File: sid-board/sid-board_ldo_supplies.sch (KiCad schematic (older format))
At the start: 12 parts, among them J1 ICM_CONN, J2 SID_CONN, J3 5V/GND, J4 3.3V/GND, J5 SPI, J6 UARTAB/IRQ, U1 SC16IS752IPW, U2 LM2596MODULE, U3 PCA82C250, U4 PCA82C250

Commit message: Working on new mostly-SMD version, switched to independant LDOs, added oscillator circuit.
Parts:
- removed U2: LM2596MODULE, sid-board:LM2596-MODULE, symbol local_symbols:LM2596MODULE
- added C2, C3: 18pF, Capacitor_SMD:C_0805_2012Metric_Pad1.15x1.40mm_HandSolder, symbol Device:C_Small
- added C4: 100nF, Capacitor_SMD:C_0805_2012Metric_Pad1.15x1.40mm_HandSolder, symbol Device:C_Small
- added R2: 1M, Resistor_SMD:R_0805_2012Metric_Pad1.15x1.40mm_HandSolder, symbol Device:R_Small
- added U2: MCP1703A-3302_SOT223, Package_TO_SOT_SMD:SOT-223-3_TabPin2, symbol Regulator_Linear:MCP1703A-3302_SOT223
- added U5: MCP1703A-5002_SOT223, Package_TO_SOT_SMD:SOT-223-3_TabPin2, symbol Regulator_Linear:MCP1703A-5002_SOT223
- added Y1: 14.7456MHz, sid-board:Euroquarts 14.7456MHz Crystal ±30ppm SMD 2-Pin 12.4 x 4.5 x 4.2mm, symbol Device:Crystal
- C1: footprint Capacitor_THT:C_Rect_L7.2mm_W2.5mm_P5.00mm_FKS2_FKP2_MKS2_MKP2 -> Capacitor_SMD:C_0805_2012Metric_Pad1.15x1.40mm_HandSolder
- J3: value 5V/GND -> 5V OUT
- J4: value 3.3V/GND -> 3.3V OUT
- R1: footprint Resistor_THT:R_Axial_DIN0207_L6.3mm_D2.5mm_P7.62mm_Horizontal -> Resistor_SMD:R_0805_2012Metric_Pad1.15x1.40mm_HandSolder
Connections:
- net labels added: XTAL1, XTAL2
- wire segments 64 -> 70
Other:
- note added: "3.3V SUPPLY LDO"
- note added: "5V SUPPLY LDO"
- note added: "TODO:\nADD XTAL1/2 OSCILLATOR CIRCUIT\nADD LDO VOLTAGE INPUT for U1"
- note added: "TOTAL ESTIMATED MAX. CURRENT = 230mA\n3.3V U1 SUPPLY = 20mA peak (2x rated max)\n5V U3/U2 SUPPLY = 210mA peak (1.5x rated max)"
- moved on the sheet: C1, J3
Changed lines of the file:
@@
 Text GLabel 2200 2500 0    50   Input ~ 0
 GND
-$Comp
-L local_symbols:LM2596MODULE U2
-U 1 1 5E29B6B7
-P 2650 4700
-F 0 "U2" H 2650 4925 50  0000 C CNN
-F 1 "LM2596MODULE" H 2650 4834 50  0000 C CNN
-F 2 "sid-board:LM2596-MODULE" H 2650 4700 50  0001 C CNN
-F 3 "" H 2650 4700 50  0001 C CNN
-	1    2650 4700
-	1    0    0    -1
-$EndComp
-Text GLabel 2150 4850 0    50   Input ~ 0
-GND
-Text GLabel 3150 4850 2    50   Input ~ 0
-GND
-Text GLabel 2150 4700 0    50   Input ~ 0
+Text GLabel 1700 5250 0    50   Input ~ 0
+GND
+Text GLabel 1400 4950 0    50   Input ~ 0
 VIN
-Text GLabel 3150 4700 2    50   Input ~ 0
+Text GLabel 3400 4950 2    50   Input ~ 0
 VDD_5V
 Text GLabel 2200 3500 0    50   Input ~ 0
@@
 L Device:C_Small C1
 U 1 1 5E2BAD29
-P 3500 3000
-F 0 "C1" V 3271 3000 50  0000 C CNN
-F 1 "100nF" V 3362 3000 50  0000 C CNN
-F 2 "Capacitor_THT:C_Rect_L7.2mm_W2.5mm_P5.00mm_FKS2_FKP2_MKS2_MKP2" H 3500 3000 50  0001 C CNN
-F 3 "~" H 3500 3000 50  0001 C CNN
-	1    3500 3000
-	0    1    1    0
-$EndComp
-Wire Wire Line
-	3950 2450 3400 2450
-Wire Wire Line
-	3600 3000 4700 3000
-Wire Wire Line
-	4700 3000 4700 2900
+P 3300 5250
+F 0 "C1" V 3071 5250 50  0000 C CNN
+F 1 "100nF" V 3162 5250 50  0000 C CNN
+F 2 "Capacitor_SMD:C_0805_2012Metric_Pad1.15x1.40mm_HandSolder" H 3300 5250 50  0001 C CNN
+F 3 "~" H 3300 5250 50  0001 C CNN
+	1    3300 5250
+	0    1    1    0
+$EndComp
 Wire Wire Line
 	3950 3300 3900 3300
@@
 Wire Wire Line
 	5500 3200 6300 3200
-Text GLabel 3800 4700 3    50   Input ~ 0
+Text GLabel 4250 4700 3    50   Input ~ 0
 VDD_5V
-Text GLabel 3900 4700 3    50   Input ~ 0
+Text GLabel 4350 4700 3    50   Input ~ 0
 GND
 Text GLabel 4850 4700 3    50   Input ~ 0
@@
 L Connector:Conn_01x02_Male J3
 U 1 1 5E30F0FD
-P 3900 4500
-F 0 "J3" V 3962 4544 50  0000 L CNN
-F 1 "5V/GND" V 4053 4544 50  0000 L CNN
-F 2 "Connector_PinHeader_2.54mm:PinHeader_1x02_P2.54mm_Vertical" H 3900 4500 50  0001 C CNN
-F 3 "~" H 3900 4500 50  0001 C CNN
-	1    3900 4500
+P 4350 4500
+F 0 "J3" V 4412 4544 50  0000 L CNN
+F 1 "5V OUT" V 4503 4544 50  0000 L CNN
+F 2 "Connector_PinHeader_2.54mm:PinHeader_1x02_P2.54mm_Vertical" H 4350 4500 50  0001 C CNN
+F 3 "~" H 4350 4500 50  0001 C CNN
+	1    4350 4500
 	0    1    1    0
 $EndComp
@@
 P 4850 4500
 F 0 "J4" V 4912 4544 50  0000 L CNN
-F 1 "3.3V/GND" V 5003 4544 50  0000 L CNN
+F 1 "3.3V OUT" V 5003 4544 50  0000 L CNN
 F 2 "Connector_PinHeader_2.54mm:PinHeader_1x02_P2.54mm_Vertical" H 4850 4500 50  0001 C CNN
 F 3 "~" H 4850 4500 50  0001 C CNN
@@
 F 0 "R1" H 6709 3846 50  0000 L CNN
 F 1 "1K" H 6709 3755 50  0000 L CNN
-F 2 "Resistor_THT:R_Axial_DIN0207_L6.3mm_D2.5mm_P7.62mm_Horizontal" H 6650 3800 50  0001 C CNN
+F 2 "Resistor_SMD:R_0805_2012Metric_Pad1.15x1.40mm_HandSolder" H 6650 3800 50  0001 C CNN
 F 3 "~" H 6650 3800 50  0001 C CNN
 	1    6650 3800
@@
 	6100 2850 6100 4000
 Wire Wire Line
-	3400 2450 3400 3000
-Wire Wire Line
-	3950 2300 3950 2450
-Wire Wire Line
 	3950 2300 3900 2300
 Wire Wire Line
 	4700 2300 4700 2350
+Text Notes 5600 2000 0    50   ~ 0
+TODO:\nADD XTAL1/2 OSCILLATOR CIRCUIT\nADD LDO VOLTAGE INPUT for U1
+Text GLabel 3100 5250 0    50   Input ~ 0
+GND
+Text GLabel 2000 4950 2    50   Input ~ 0
+VDD_3.3V
+Text Notes 1450 4450 0    50   ~ 0
+TOTAL ESTIMATED MAX. CURRENT = 230mA\n3.3V U1 SUPPLY = 20mA peak (2x rated max)\n5V U3/U2 SUPPLY = 210mA peak (1.5x rated max)
+$Comp
+L Regulator_Linear:MCP1703A-3302_SOT223 U2
+U 1 1 5E2845BD
+P 1700 4950
+F 0 "U2" H 1700 5192 50  0000 C CNN
+F 1 "MCP1703A-3302_SOT223" H 1700 5101 50  0000 C CNN
+F 2 "Package_TO_SOT_SMD:SOT-223-3_TabPin2" H 1700 5150 50  0001 C CNN
+F 3 "http://ww1.microchip.com/downloads/en/DeviceDoc/20005122B.pdf" H 1700 4900 50  0001 C CNN
+	1    1700 4950
+	1    0    0    -1
+$EndComp
+$Comp
+L Regulator_Linear:MCP1703A-5002_SOT223 U5
+U 1 1 5E285FEA
+P 3100 4950
+F 0 "U5" H 3100 5192 50  0000 C CNN
+F 1 "MCP1703A-5002_SOT223" H 3100 5101 50  0000 C CNN
+F 2 "Package_TO_SOT_SMD:SOT-223-3_TabPin2" H 3100 5150 50  0001 C CNN
+F 3 "http://ww1.microchip.com/downloads/en/DeviceDoc/20005122B.pdf" H 3100 4900 50  0001 C CNN
+	1    3100 4950
+	1    0    0    -1
+$EndComp
+Text GLabel 2800 4950 0    50   Input ~ 0
+VIN
+Text Notes 1400 4650 0    50   ~ 10
+3.3V SUPPLY LDO
+Text Notes 2800 4650 0    50   ~ 10
+5V SUPPLY LDO
+$Comp
+L Device:Crystal Y1
+U 1 1 5E2B8361
+P 7400 3000
+F 0 "Y1" H 7400 3268 50  0000 C CNN
+F 1 "14.7456MHz" H 7400 3177 50  0000 C CNN
+F 2 "sid-board:Euroquarts 14.7456MHz Crystal ±30ppm SMD 2-Pin 12.4 x 4.5 x 4.2mm" H 7400 3000 50  0001 C CNN
+F 3 "~" H 7400 3000 50  0001 C CNN
+	1    7400 3000
+	1    0    0    -1
+$EndComp
+$Comp
+L Device:R_Small R2
+U 1 1 5E2B87B7
+P 7400 3350
+F 0 "R2" V 7204 3350 50  0000 C CNN
+F 1 "1M" V 7295 3350 50  0000 C CNN
+F 2 "Resistor_SMD:R_0805_2012Metric_Pad1.15x1.40mm_HandSolder" H 7400 3350 50  0001 C CNN
+F 3 "~" H 7400 3350 50  0001 C CNN
+	1    7400 3350
+	0    1    1    0
+$EndComp
+$Comp
+L Device:C_Small C2
+U 1 1 5E2B9259
+P 7250 3600
+F 0 "C2" H 7342 3646 50  0000 L CNN
+F 1 "18pF" H 7342 3555 50  0000 L CNN
+F 2 "Capacitor_SMD:C_0805_2012Metric_Pad1.15x1.40mm_HandSolder" H 7250 3600 50  0001 C CNN
+F 3 "~" H 7250 3600 50  0001 C CNN
+	1    7250 3600
+	1    0    0    -1
+$EndComp
+$Comp
+L Device:C_Small C3
+U 1 1 5E2BA581
+P 7550 3600
+F 0 "C3" H 7642 3646 50  0000 L CNN
+F 1 "18pF" H 7642 3555 50  0000 L CNN
+F 2 "Capacitor_SMD:C_0805_2012Metric_Pad1.15x1.40mm_HandSolder" H 7550 3600 50  0001 C CNN
+F 3 "~" H 7550 3600 50  0001 C CNN
+	1    7550 3600
+	1    0    0    -1
+$EndComp
+Wire Wire Line
+	7250 3000 7250 3350
+Wire Wire Line
+	7250 3350 7300 3350
+Wire Wire Line
+	7250 3350 7250 3500
+Connection ~ 7250 3350
+Wire Wire Line
+	7550 3000 7550 3350
+Wire Wire Line
+	7550 3350 7500 3350
+Wire Wire Line
+	7250 3700 7550 3700
+Wire Wire Line
+	7550 3350 7550 3500
+Connection ~ 7550 3350
+Text GLabel 7400 3700 3    50   Input ~ 0
+GND
+Text GLabel 7550 3000 2    50   Input ~ 10
+XTAL1
+Text GLabel 7250 3000 0    50   Input ~ 10
+XTAL2
+Text GLabel 5500 2900 0    50   Input ~ 10
+XTAL1
+Text GLabel 5500 3000 0    50   Input ~ 10
+XTAL2
+$Comp
+L Device:C_Small C4
+U 1 1 5E29894F
+P 1900 5250
+F 0 "C4" V 1671 5250 50  0000 C CNN
+F 1 "100nF" V 1762 5250 50  0000 C CNN
+F 2 "Capacitor_SMD:C_0805_2012Metric_Pad1.15x1.40mm_HandSolder" H 1900 5250 50  0001 C CNN
+F 3 "~" H 1900 5250 50  0001 C CNN
+	1    1900 5250
+	0    1    1    0
+$EndComp
+Wire Wire Line
+	2000 4950 2000 5250
+Wire Wire Line
+	1800 5250 1700 5250
+Wire Wire Line
+	3100 5250 3200 5250
+Wire Wire Line
+	3400 5250 3400 4950
 $EndSCHEMATC

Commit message: Re-did PCB layout, signifcantly smaller now.
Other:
- note removed: "TODO:\nADD XTAL1/2 OSCILLATOR CIRCUIT\nADD LDO VOLTAGE INPUT for U1"
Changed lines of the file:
@@
 Wire Wire Line
 	4700 2300 4700 2350
-Text Notes 5600 2000 0    50   ~ 0
-TODO:\nADD XTAL1/2 OSCILLATOR CIRCUIT\nADD LDO VOLTAGE INPUT for U1
 Text GLabel 3100 5250 0    50   Input ~ 0
 GND

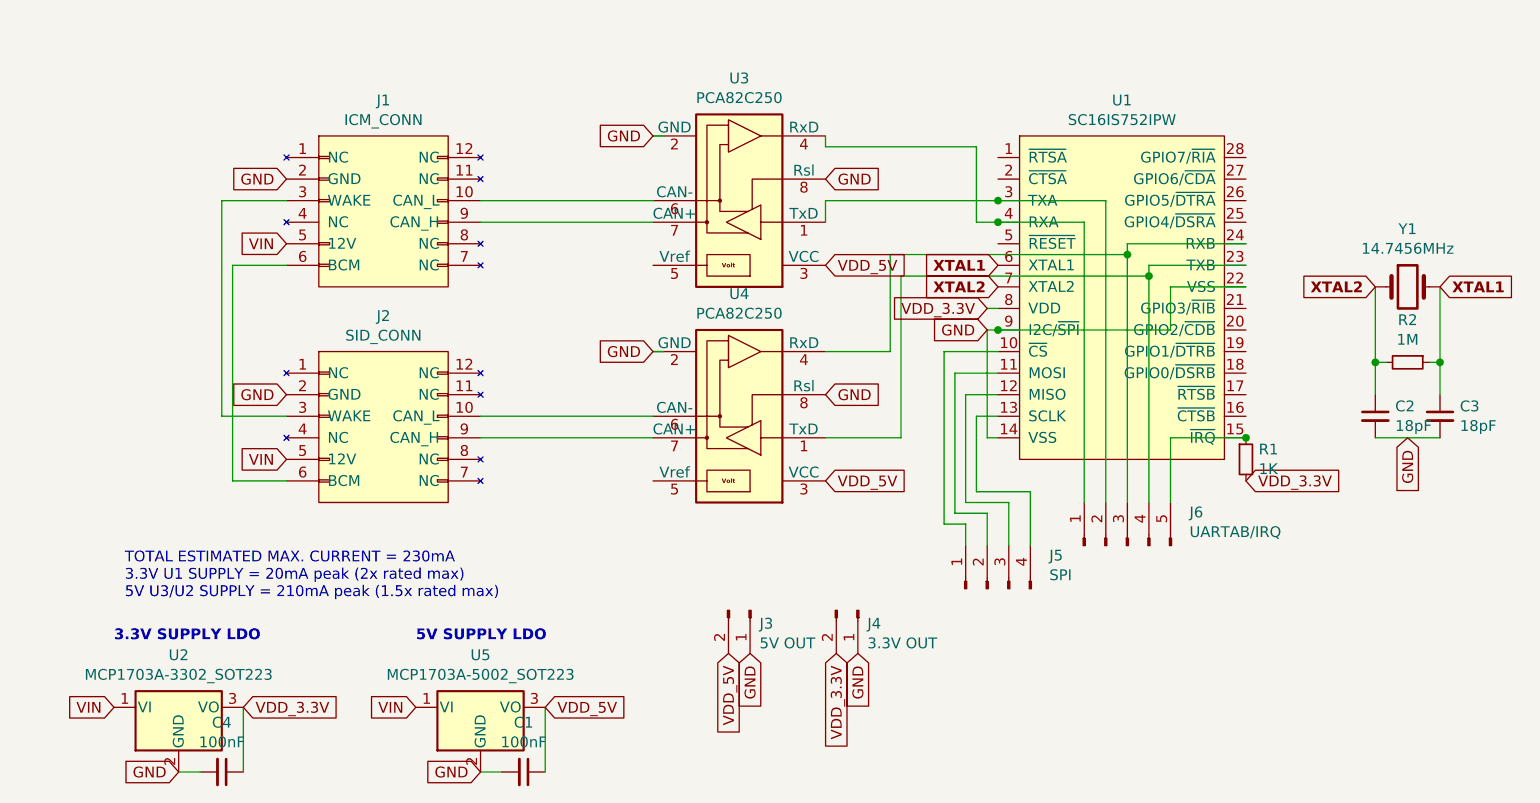
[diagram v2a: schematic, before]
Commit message: Autorouted vs Manual routed. Thinking about adding DIP switch.
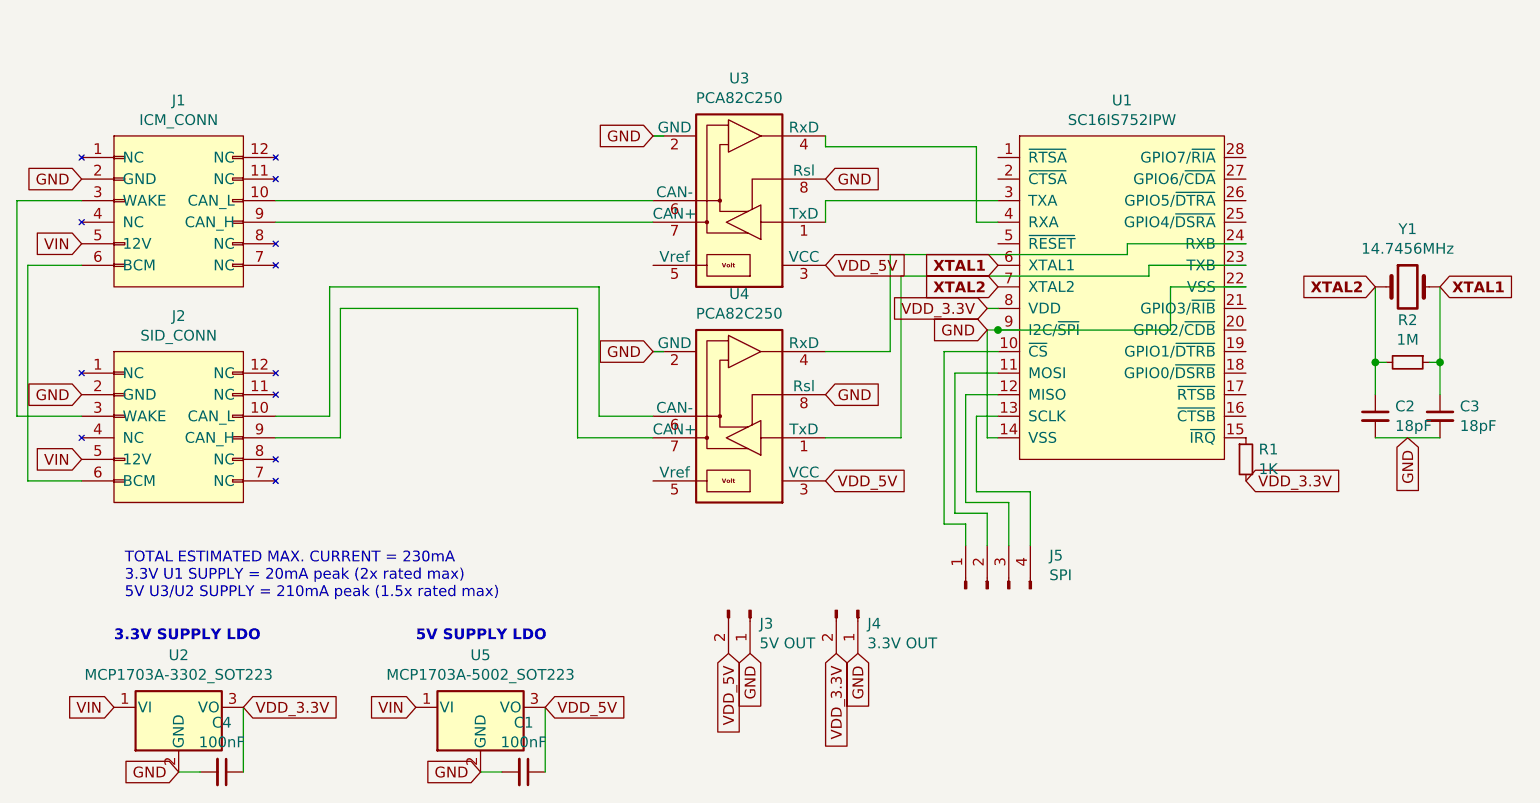
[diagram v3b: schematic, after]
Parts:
- removed J6: UARTAB/IRQ, Connector_PinHeader_2.54mm:PinHeader_1x05_P2.54mm_Vertical, symbol Connector:Conn_01x05_Male
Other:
- moved on the sheet: J1, J2
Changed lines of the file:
@@
 L local_symbols:Conn_02x06_SAAB_SID_HPD J1
 U 1 1 5E210180
-P 2650 2600
-F 0 "J1" H 2650 3065 50  0000 C CNN
-F 1 "ICM_CONN" H 2650 2974 50  0000 C CNN
-F 2 "sid-board:SAAB_SID_CONNECTOR_HEADER" H 2400 2600 50  0001 C CNN
-F 3 "~" H 2400 2600 50  0001 C CNN
-	1    2650 2600
+P 1700 2600
+F 0 "J1" H 1700 3065 50  0000 C CNN
+F 1 "ICM_CONN" H 1700 2974 50  0000 C CNN
+F 2 "sid-board:SAAB_SID_CONNECTOR_HEADER" H 1450 2600 50  0001 C CNN
+F 3 "~" H 1450 2600 50  0001 C CNN
+	1    1700 2600
 	1    0    0    -1
 $EndComp
@@
 L local_symbols:Conn_02x06_SAAB_SID_HPD J2
 U 1 1 5E211BEE
-P 2650 3600
-F 0 "J2" H 2650 4065 50  0000 C CNN
-F 1 "SID_CONN" H 2650 3974 50  0000 C CNN
-F 2 "sid-board:SAAB_SID_CONNECTOR_HEADER" H 2400 3600 50  0001 C CNN
-F 3 "~" H 2400 3600 50  0001 C CNN
-	1    2650 3600
-	1    0    0    -1
-$EndComp
-Text GLabel 2200 2800 0    50   Input ~ 0
+P 1700 3600
+F 0 "J2" H 1700 4065 50  0000 C CNN
+F 1 "SID_CONN" H 1700 3974 50  0000 C CNN
+F 2 "sid-board:SAAB_SID_CONNECTOR_HEADER" H 1450 3600 50  0001 C CNN
+F 3 "~" H 1450 3600 50  0001 C CNN
+	1    1700 3600
+	1    0    0    -1
+$EndComp
+Text GLabel 1250 2800 0    50   Input ~ 0
 VIN
-Text GLabel 2200 2500 0    50   Input ~ 0
+Text GLabel 1250 2500 0    50   Input ~ 0
 GND
 Text GLabel 1700 5250 0    50   Input ~ 0
@@
 Text GLabel 3400 4950 2    50   Input ~ 0
 VDD_5V
-Text GLabel 2200 3500 0    50   Input ~ 0
-GND
-Text GLabel 2200 3800 0    50   Input ~ 0
+Text GLabel 1250 3500 0    50   Input ~ 0
+GND
+Text GLabel 1250 3800 0    50   Input ~ 0
 VIN
 Wire Wire Line
-	2200 2900 1950 2900
-Wire Wire Line
-	1950 2900 1950 3900
-Wire Wire Line
-	1950 3900 2200 3900
-Wire Wire Line
-	2200 3600 1900 3600
-Wire Wire Line
-	1900 3600 1900 2600
-Wire Wire Line
-	1900 2600 2200 2600
+	1250 2900 1000 2900
+Wire Wire Line
+	1000 2900 1000 3900
+Wire Wire Line
+	1000 3900 1250 3900
+Wire Wire Line
+	1250 3600 950  3600
+Wire Wire Line
+	950  3600 950  2600
+Wire Wire Line
+	950  2600 1250 2600
 $Comp
 L local_symbols:PCA82C250 U4
@@
 	-1   0    0    1
 $EndComp
-Wire Wire Line
-	3100 2600 3900 2600
-Wire Wire Line
-	3900 2700 3100 2700
-Wire Wire Line
-	3100 3600 3900 3600
-Wire Wire Line
-	3900 3700 3100 3700
 Text GLabel 3900 2300 0    50   Input ~ 0
 GND
@@
 	0    1    1    0
 $EndComp
-$Comp
-L Connector:Conn_01x05_Male J6
-U 1 1 5E325875
-P 6100 4200
-F 0 "J6" V 6254 3912 50  0000 R CNN
-F 1 "UARTAB/IRQ" V 6163 3912 50  0000 R CNN
-F 2 "Connector_PinHeader_2.54mm:PinHeader_1x05_P2.54mm_Vertical" H 6100 4200 50  0001 C CNN
-F 3 "~" H 6100 4200 50  0001 C CNN
-	1    6100 4200
-	0    -1   -1   0
-$EndComp
-Wire Wire Line
-	5900 2700 5900 4000
-Wire Wire Line
-	5500 2600 6000 2600
-Wire Wire Line
-	6000 2600 6000 4000
 Wire Wire Line
 	6650 2800 6100 2800
@@
 Wire Wire Line
 	6650 2900 6200 2900
-Wire Wire Line
-	6650 3700 6300 3700
-Wire Wire Line
-	6300 3700 6300 4000
 $Comp
 L Device:R_Small R1
@@
 	1    0    0    -1
 $EndComp
-Connection ~ 6650 3700
 Text GLabel 6650 3900 2    50   Input ~ 0
 VDD_3.3V
@@
 Wire Wire Line
 	4700 2600 5500 2600
-Connection ~ 5500 2600
 Wire Wire Line
 	4700 2350 5400 2350
@@
 Wire Wire Line
 	5400 2700 5500 2700
-Connection ~ 5500 2700
-Wire Wire Line
-	5500 2700 5900 2700
 Wire Wire Line
 	6200 2900 6200 2950
@@
 Wire Wire Line
 	5050 2950 6200 2950
-Connection ~ 6200 2950
-Wire Wire Line
-	6200 2950 6200 4000
 Wire Wire Line
 	4700 3300 5000 3300
@@
 Wire Wire Line
 	5000 2850 5000 3300
-Connection ~ 6100 2850
-Wire Wire Line
-	6100 2850 6100 4000
 Wire Wire Line
 	3950 2300 3900 2300
@@
 Wire Wire Line
 	3400 5250 3400 4950
+Wire Wire Line
+	2150 3600 2400 3600
+Wire Wire Line
+	2400 3600 2400 3000
+Wire Wire Line
+	2150 3700 2450 3700
+Wire Wire Line
+	2450 3700 2450 3100
+Wire Wire Line
+	3550 3100 3550 3700
+Wire Wire Line
+	3650 3600 3900 3600
+Wire Wire Line
+	3550 3700 3900 3700
+Wire Wire Line
+	2150 2600 3900 2600
+Wire Wire Line
+	2150 2700 3900 2700
+Wire Wire Line
+	3650 3000 3650 3600
+Wire Wire Line
+	2400 3000 3650 3000
+Wire Wire Line
+	2450 3100 3550 3100
 $EndSCHEMATC

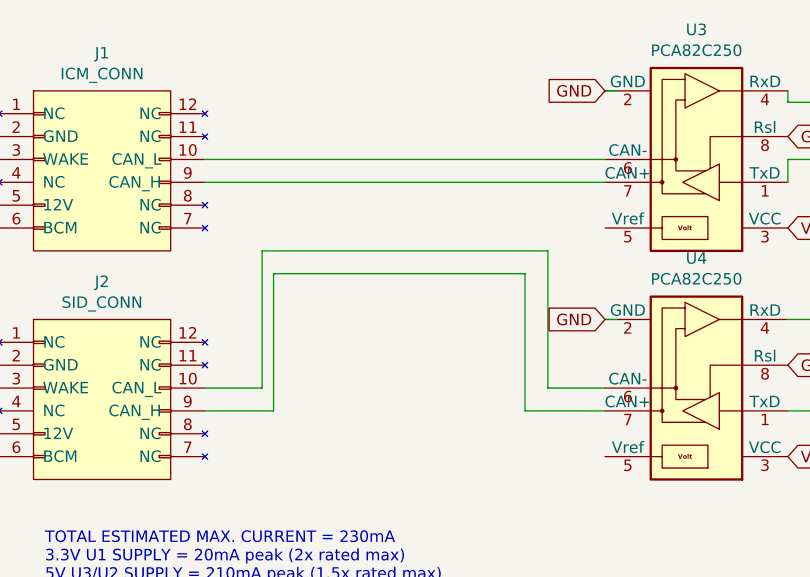
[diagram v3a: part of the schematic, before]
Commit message: Added bypass DIP switch
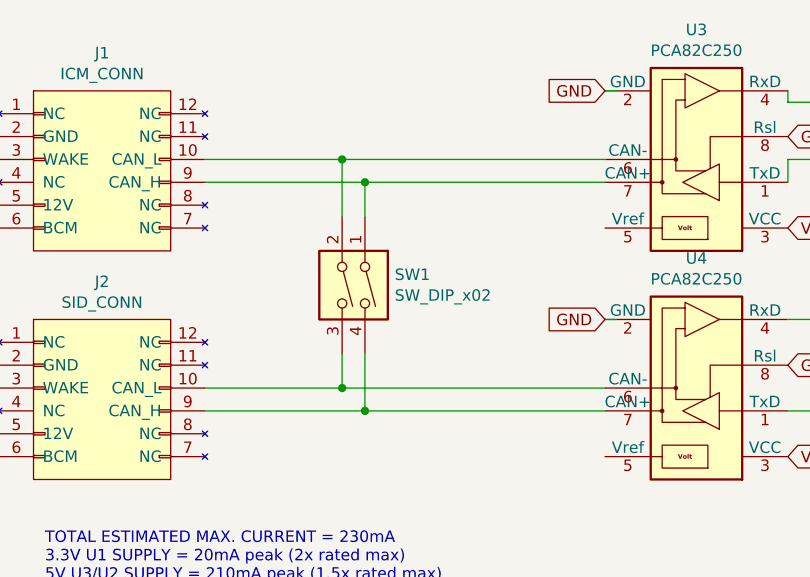
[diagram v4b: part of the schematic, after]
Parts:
- added SW1: SW_DIP_x02, Button_Switch_THT:SW_DIP_SPSTx02_Slide_9.78x7.26mm_W7.62mm_P2.54mm, symbol Switch:SW_DIP_x02
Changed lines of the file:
@@
 	3400 5250 3400 4950
 Wire Wire Line
-	2150 3600 2400 3600
+	2150 2600 2750 2600
 Wire Wire Line
-	2400 3600 2400 3000
+	2150 2700 2850 2700
 Wire Wire Line
-	2150 3700 2450 3700
+	2150 3600 2750 3600
 Wire Wire Line
-	2450 3700 2450 3100
+	2150 3700 2850 3700
+$Comp
+L Switch:SW_DIP_x02 SW1
+U 1 1 5E28AC65
+P 2750 3150
+F 0 "SW1" V 2704 3380 50  0000 L CNN
+F 1 "SW_DIP_x02" V 2795 3380 50  0000 L CNN
+F 2 "Button_Switch_THT:SW_DIP_SPSTx02_Slide_9.78x7.26mm_W7.62mm_P2.54mm" H 2750 3150 50  0001 C CNN
+F 3 "~" H 2750 3150 50  0001 C CNN
+	1    2750 3150
+	0    1    1    0
+$EndComp
 Wire Wire Line
-	3550 3100 3550 3700
+	2750 2850 2750 2600
+Connection ~ 2750 2600
 Wire Wire Line
-	3650 3600 3900 3600
+	2750 2600 3900 2600
 Wire Wire Line
-	3550 3700 3900 3700
+	2850 2850 2850 2700
+Connection ~ 2850 2700
 Wire Wire Line
-	2150 2600 3900 2600
+	2850 2700 3900 2700
 Wire Wire Line
-	2150 2700 3900 2700
+	2750 3450 2750 3600
+Connection ~ 2750 3600
 Wire Wire Line
-	3650 3000 3650 3600
+	2750 3600 3900 3600
 Wire Wire Line
-	2400 3000 3650 3000
+	2850 3450 2850 3700
+Connection ~ 2850 3700
 Wire Wire Line
-	2450 3100 3550 3100
+	2850 3700 3900 3700
 $EndSCHEMATC
